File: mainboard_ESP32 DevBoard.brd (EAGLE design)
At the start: 54.9 x 106.7 mm, 44 parts, among them IC1 OP-AMP-2-LONG, K1 AQH213, T1 2N2222, X1 JST-XH-02-PIN-LONG-PAD, X2 JST-XH-04-PIN-LONG-PAD, X3 1751293, X4 JST-XH-04-PIN-LONG-PAD

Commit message: Corrected some component values that were wrong during assembly
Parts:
- R12: value 40K -> 39k
- R4, R5: value 750 -> 12k
- R6: value 1.3K -> 1.2k
- R8: value 750 -> 330
- moved X2 2.54 mm to (52.1, 36.8)
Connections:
- net ENER_COIL: now also K1.6, U$5.P$2; no longer K1.8, U$5.P$1
- net VACL: now also K1.8, U$5.P$1; no longer K1.6, U$5.P$2
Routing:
- net VACL: track 53.7 -> 38.2 mm
- net ENER_COIL: track 19.2 -> 14.2 mm
- net GFI_TEST: track 12.3 -> 15.5 mm
- net CT: track 22.6 -> 25.1 mm
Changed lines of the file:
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@@
 <attribute name="VALUE" x="48.7426" y="21.2344" size="0.9906" layer="27" ratio="10" rot="R90"/>
 </element>
-<element name="R12" library="Passive" package="0204/7-L" value="40K" x="41.91" y="42.926" smashed="yes" rot="R270">
+<element name="R12" library="Passive" package="0204/7-L" value="39k" x="41.91" y="42.926" smashed="yes" rot="R270">
 <attribute name="NAME" x="43.7134" y="39.624" size="0.9906" layer="25" font="vector" ratio="10" rot="R270" align="center"/>
 <attribute name="VALUE" x="41.4274" y="43.2816" size="0.9906" layer="27" ratio="10" rot="R270"/>
@@
 <attribute name="VALUE" x="48.1775" y="8.1275" size="1.016" layer="27" ratio="10" rot="R90"/>
 </element>
-<element name="X2" library="Rembrandt Electronics - JST XH Connectors v1-0" package="JST-XH-04-PACKAGE-LONG-PAD" value="JST-XH-04-PIN-LONG-PAD" x="52.07" y="34.29" smashed="yes" rot="R90">
-<attribute name="NAME" x="47.701" y="37.584" size="1.016" layer="25" font="vector" ratio="10" rot="R90" align="center"/>
-<attribute name="VALUE" x="48.1775" y="28.2875" size="1.016" layer="27" ratio="10" rot="R90"/>
+<element name="X2" library="Rembrandt Electronics - JST XH Connectors v1-0" package="JST-XH-04-PACKAGE-LONG-PAD" value="JST-XH-04-PIN-LONG-PAD" x="52.07" y="36.83" smashed="yes" rot="R90">
+<attribute name="NAME" x="47.701" y="40.124" size="1.016" layer="25" font="vector" ratio="10" rot="R90" align="center"/>
+<attribute name="VALUE" x="48.1775" y="30.8275" size="1.016" layer="27" ratio="10" rot="R90"/>
 </element>
 <element name="JP1" library="pinhead" library_urn="urn:adsk.eagle:library:325" package="1X02" package3d_urn="urn:adsk.eagle:package:22435/2" value="" x="20.32" y="58.42" smashed="yes" rot="R270">
@@
 <attribute name="VALUE" x="26.67" y="8.255" size="1.27" layer="27" rot="R180"/>
 </element>
-<element name="R8" library="Passive" package="0204/7-L" value="750" x="45.72" y="22.86" smashed="yes" rot="R270">
+<element name="R8" library="Passive" package="0204/7-L" value="330" x="45.72" y="22.86" smashed="yes" rot="R270">
 <attribute name="NAME" x="43.9674" y="24.384" size="0.9906" layer="25" font="vector" ratio="10" rot="R270" align="center"/>
 <attribute name="VALUE" x="45.2374" y="24.4856" size="0.9906" layer="27" ratio="10" rot="R270"/>
@@
 <attribute name="VALUE" x="38.1" y="61.849" size="1.778" layer="27" ratio="10" rot="R180"/>
 </element>
-<element name="R4" library="Passive" package="0204/7-L" value="750" x="43.18" y="55.372" smashed="yes" rot="R270">
+<element name="R4" library="Passive" package="0204/7-L" value="12k" x="43.18" y="55.372" smashed="yes" rot="R270">
 <attribute name="NAME" x="40.9194" y="56.388" size="0.9906" layer="25" ratio="10" rot="R270"/>
 <attribute name="VALUE" x="42.6974" y="56.9976" size="0.9906" layer="27" ratio="10" rot="R270"/>
 </element>
-<element name="R5" library="Passive" package="0204/7-L" value="750" x="45.72" y="53.594" smashed="yes" rot="R270">
+<element name="R5" library="Passive" package="0204/7-L" value="12k" x="45.72" y="53.594" smashed="yes" rot="R270">
 <attribute name="NAME" x="43.9674" y="58.42" size="0.9906" layer="25" ratio="10" rot="R270"/>
 <attribute name="VALUE" x="45.2374" y="55.2196" size="0.9906" layer="27" ratio="10" rot="R270"/>
@@
 <attribute name="VALUE" x="39.116" y="21.717" size="1.27" layer="27" ratio="10" rot="R180"/>
 </element>
-<element name="R6" library="Passive" package="0204/7-L" value="1.3K" x="36.83" y="24.13" smashed="yes" rot="R180">
+<element name="R6" library="Passive" package="0204/7-L" value="1.2k" x="36.83" y="24.13" smashed="yes" rot="R180">
 <attribute name="NAME" x="39.37" y="22.8346" size="0.9906" layer="25" ratio="10" rot="R180"/>
 <attribute name="VALUE" x="38.4556" y="24.6126" size="0.9906" layer="27" ratio="10" rot="R180"/>
@@
 <contactref element="X2" pad="1"/>
 <contactref element="IC1" pad="3"/>
-<wire x1="50.8" y1="26.67" x2="50.8" y2="29.21" width="0.762" layer="16"/>
-<wire x1="50.8" y1="29.21" x2="52.07" y2="30.48" width="0.762" layer="16"/>
+<wire x1="50.8" y1="26.67" x2="50.8" y2="31.75" width="0.762" layer="16"/>
+<wire x1="50.8" y1="31.75" x2="52.07" y2="33.02" width="0.762" layer="16"/>
 <wire x1="38.7462" y1="23.61745" x2="39.47105" y2="22.8926" width="0.762" layer="16"/>
 <wire x1="38.1" y1="26.67" x2="38.7462" y2="26.0238" width="0.762" layer="16"/>
@@
 <contactref element="X2" pad="3"/>
 <contactref element="R8" pad="1"/>
-<wire x1="50.8" y1="35.56" x2="52.07" y2="35.56" width="0.762" layer="16"/>
 <wire x1="45.72" y1="26.67" x2="48.26" y2="29.21" width="0.762" layer="16"/>
-<wire x1="48.26" y1="29.21" x2="48.26" y2="33.02" width="0.762" layer="16"/>
-<wire x1="48.26" y1="33.02" x2="50.8" y2="35.56" width="0.762" layer="16"/>
+<wire x1="48.26" y1="36.83" x2="49.53" y2="38.1" width="0.762" layer="16"/>
+<wire x1="49.53" y1="38.1" x2="52.07" y2="38.1" width="0.762" layer="16"/>
+<wire x1="48.26" y1="29.21" x2="48.26" y2="36.83" width="0.762" layer="16"/>
 </signal>
 <signal name="ENER_COIL" class="1">
-<contactref element="K1" pad="8"/>
 <contactref element="X3" pad="4"/>
-<wire x1="50.9" y1="58.42" x2="47.331" y2="61.989" width="0.762" layer="16"/>
-<contactref element="U$5" pad="P$1"/>
-<wire x1="47.331" y1="66.929" x2="44.45" y2="69.81" width="0.762" layer="16"/>
-<wire x1="47.331" y1="61.989" x2="47.331" y2="66.929" width="0.762" layer="16"/>
-<wire x1="44.45" y1="69.81" x2="39.41" y2="69.81" width="0.762" layer="16"/>
-<wire x1="39.41" y1="69.81" x2="39.37" y2="69.85" width="0.762" layer="16"/>
+<contactref element="K1" pad="6"/>
+<contactref element="U$5" pad="P$2"/>
+<wire x1="50.9" y1="58.42" x2="44.51" y2="64.81" width="0.762" layer="16"/>
+<wire x1="44.51" y1="64.81" x2="44.45" y2="64.81" width="0.762" layer="16"/>
+<wire x1="39.37" y1="64.77" x2="39.41" y2="64.81" width="0.762" layer="16"/>
+<wire x1="39.41" y1="64.81" x2="44.45" y2="64.81" width="0.762" layer="16"/>
 </signal>
 <signal name="DHT_DATA">
@@
 <signal name="VACL" class="1">
 <contactref element="PS1" pad="2"/>
-<contactref element="K1" pad="6"/>
-<wire x1="50.8" y1="79.07586875" x2="50.8" y2="95.21" width="0.762" layer="16"/>
+<wire x1="50.8" y1="95.21" x2="50.8" y2="79.07586875" width="0.762" layer="16"/>
+<contactref element="X3" pad="7"/>
+<contactref element="K1" pad="8"/>
+<contactref element="U$5" pad="P$1"/>
+<wire x1="44.45" y1="69.81" x2="39.41" y2="69.81" width="0.762" layer="16"/>
+<wire x1="39.41" y1="69.81" x2="39.37" y2="69.85" width="0.762" layer="16"/>
 <wire x1="48.244" y1="76.51986875" x2="50.8" y2="79.07586875" width="0.762" layer="16"/>
-<wire x1="48.244" y1="73.66" x2="48.244" y2="76.51986875" width="0.762" layer="16"/>
-<contactref element="X3" pad="7"/>
-<wire x1="50.9" y1="68.92" x2="48.244" y2="71.576" width="0.762" layer="16"/>
-<wire x1="48.244" y1="71.576" x2="48.244" y2="73.66" width="0.762" layer="16"/>
-<contactref element="U$5" pad="P$2"/>
-<wire x1="39.3748875" y1="73.66" x2="36.489" y2="70.7741125" width="0.762" layer="16"/>
-<wire x1="36.489" y1="67.651" x2="39.37" y2="64.77" width="0.762" layer="16"/>
-<wire x1="48.244" y1="73.66" x2="39.3748875" y2="73.66" width="0.762" layer="16"/>
-<wire x1="36.489" y1="70.7741125" x2="36.489" y2="67.651" width="0.762" layer="16"/>
-<wire x1="44.45" y1="64.81" x2="44.41" y2="64.77" width="0.762" layer="16"/>
-<wire x1="44.41" y1="64.77" x2="39.37" y2="64.77" width="0.762" layer="16"/>
+<wire x1="44.45" y1="69.81" x2="44.49" y2="69.85" width="0.762" layer="16"/>
+<wire x1="44.49" y1="69.85" x2="46.99" y2="69.85" width="0.762" layer="16"/>
+<wire x1="46.99" y1="69.85" x2="48.244" y2="71.104" width="0.762" layer="16"/>
+<wire x1="48.244" y1="71.104" x2="48.244" y2="76.51986875" width="0.762" layer="16"/>
+<wire x1="50.9" y1="68.92" x2="50.428" y2="68.92" width="0.762" layer="16"/>
+<wire x1="50.428" y1="68.92" x2="48.244" y2="71.104" width="0.762" layer="16"/>
 </signal>
 <signal name="VACN" class="1">

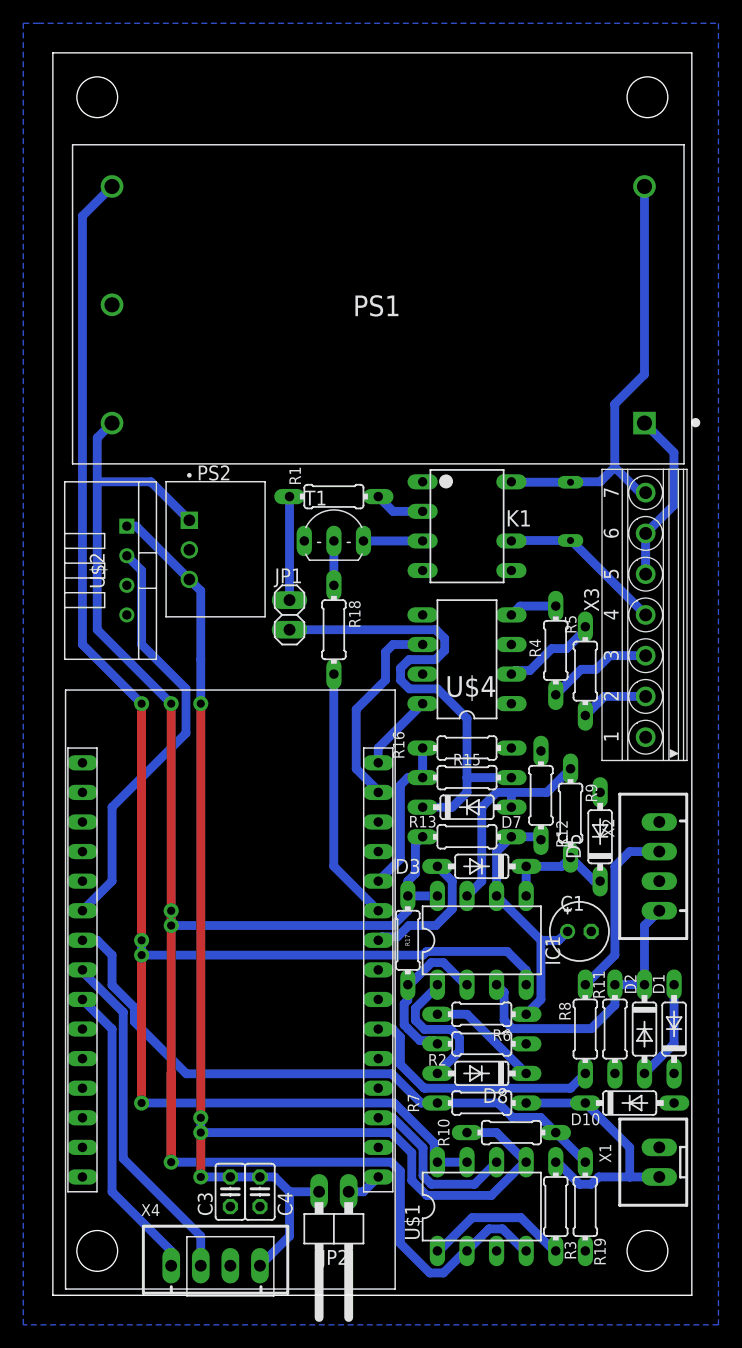
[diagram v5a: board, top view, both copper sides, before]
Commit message: Creating the BOM on digikey uncovered some footprint mismatches. They havee been corrected
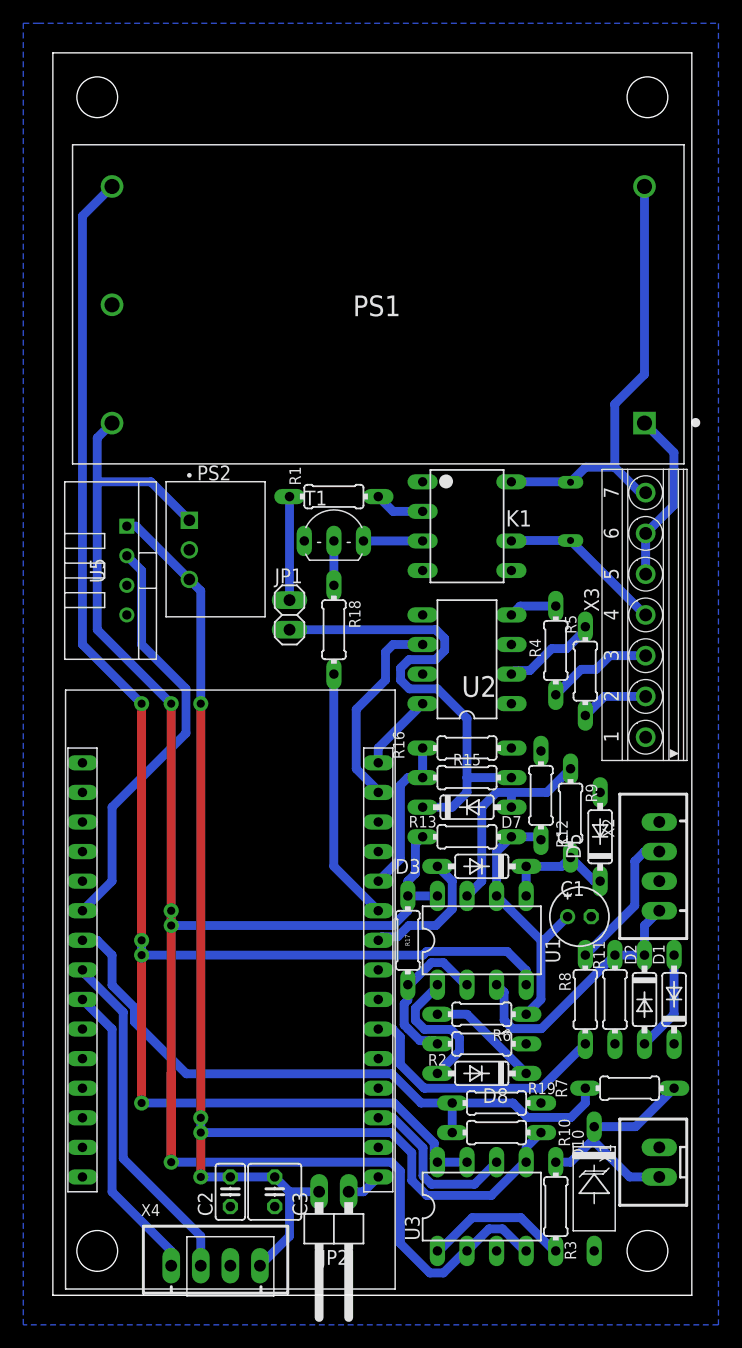
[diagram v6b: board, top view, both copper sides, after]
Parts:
- removed C4: 10uF, rcl:C025-025X050
- removed IC1: OP-AMP-2-LONG, Op Amp:DIL08-LONG
- removed U$1: DG419DJ-L, Analog Switches:DIL08-LONG
- removed U$4: OPTOCOUPLER-2, optocouplers:DIL8
- added C2: 0.1uF, rcl:C025-025X050
- added U1: LM833N, EVSE:DIL08-LONG
- added U2: ILD620GB, EVSE:DIL8
- added U3: DG419DJ-L, EVSE:DIL08-LONG
- C3: value 0.1uF -> 10uF; device rcl:C025-025X050 -> rcl:C025-050X050
- D10: value TVS 12.1V -> 12.1V; device Passive:DO35-7 -> EVSE:DO15
- D5: value 8V -> 8.2V
- MOV1: value MOV-07D391K -> MOV-07D471K
- PS1: device RAC20-12DK:CONV_RAC20-12DK -> EVSE:CONV_RAC20-12DK
- PS2: device R-78E3.3-0.5:CONV_R-78E3.3-0.5 -> EVSE:CONV_R-78E3.3-0.5
- moved R7 12.8 mm to (49.5, 17.8)
- moved R19 11.7 mm to (38.1, 16.5), turned to 180 degrees
- moved D10 7.97 mm to (46.5, 9.14), turned to 270 degrees
- moved C3 3.81 mm to (19.1, 8.89)
- moved D1 2.54 mm to (53.3, 25.4)
- moved D2 2.54 mm to (50.8, 25.4)
- moved R11 2.54 mm to (48.3, 25.4)
- moved R8 2.54 mm to (45.7, 25.4)
- moved C1 1.27 mm to (45.2, 32.5)
- moved R10 1.27 mm to (38.1, 14.0), turned to 180 degrees
- renumbered U$2 to U5, U$3 to U4, U$5 to MOV1
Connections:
- net +12V: now also U1.8, U3.2, U3.4; no longer IC1.8, U$1.2, U$1.4
- net +3V3: now also C2.1, U3.5; no longer C4.1, U$1.5
- net -12V: now also U1.4, U3.7, U3.8; no longer IC1.4, U$1.7, U$1.8
- net CP_PWM: now also U3.6; no longer U$1.6
- net CT: now also U1.3; no longer IC1.3
- net GND: now also C2.2, U2.1, U2.3, U2.5, U2.7, U3.3; no longer C4.2, U$1.3, U$4.1, U$4.3, U$4.5, U$4.7
- net N$13: now also U1.5; no longer IC1.5
- net N$15: now also U1.1; no longer IC1.1
- net N$16: now also U2.2; no longer U$4.2
- net N$17: now also U2.4; no longer U$4.4
- net N$2: now also U1.2; no longer IC1.2
- net N$4: now also U1.7; no longer IC1.7
- net N$8: now also U3.1; no longer U$1.1
- net N$9: now also U1.6; no longer IC1.6
- net VACL_SENS: now also U2.6; no longer U$4.6
- net VACN_SENS: now also U2.8; no longer U$4.8
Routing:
- net GFI_TEST: track 15.5 -> 12.3 mm
- net +3V3: track 115.9 -> 112.9 mm
- net CP_READ: track 53.3 -> 56.0 mm
- net CT: track 25.1 -> 22.6 mm
- net CP: track 22.9 -> 21.5 mm
- net GFI_TST_SIG: track 21.8 -> 22.9 mm
- net N$9: track 23.1 -> 23.6 mm

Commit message: Added pullup resistors for I2C bus
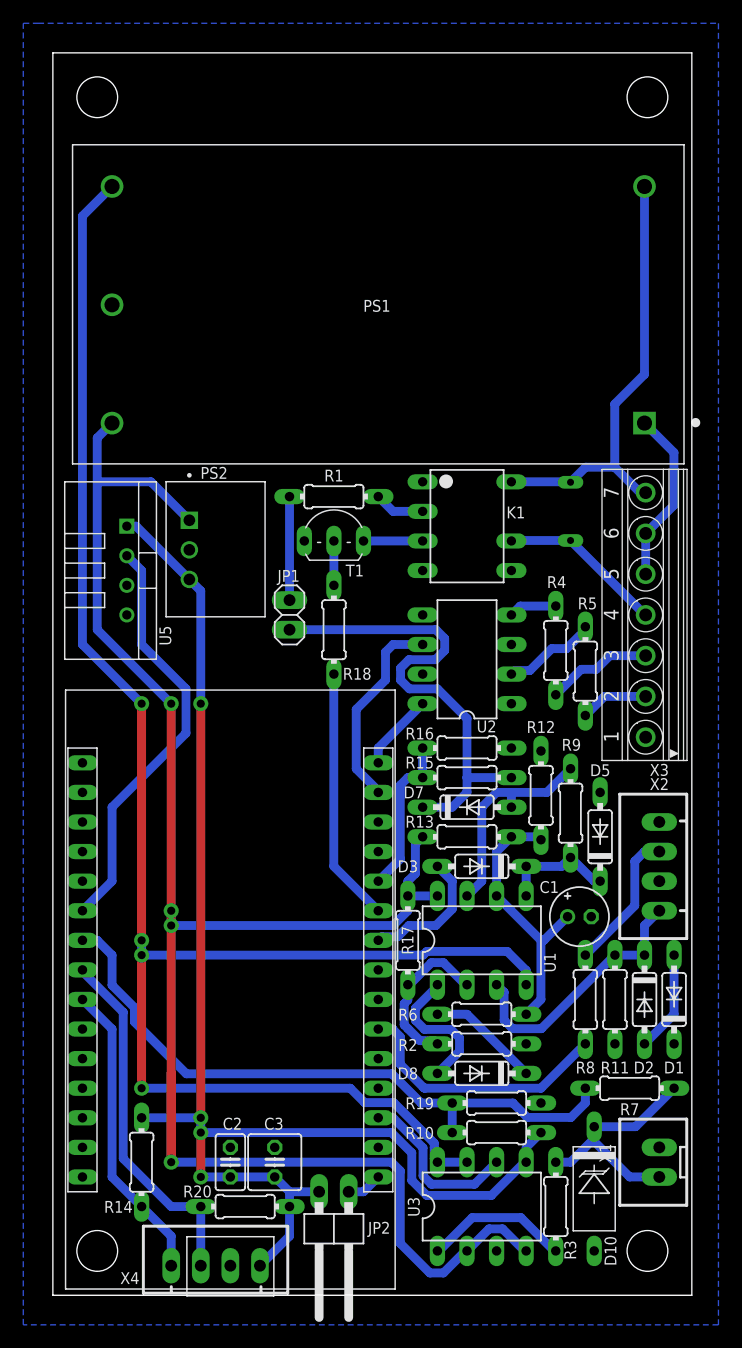
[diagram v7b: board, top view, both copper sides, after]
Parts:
- added R14, R20: 2.4K, Passive:0204/7-L
- moved C2 2.54 mm to (15.2, 11.4), turned to 90 degrees
- moved C3 2.54 mm to (19.1, 11.4), turned to 90 degrees
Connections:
- net +3V3: now also R14.2, R20.2
- net SCL: now also R14.1
- net SDA: now also R20.1
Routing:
- net +3V3: track 112.9 -> 118.0 mm
- net SDA: track 29.6 -> 31.1 mm
- net -12V: track 147.7 -> 147.0 mm
